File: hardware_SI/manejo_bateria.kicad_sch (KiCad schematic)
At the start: 6 parts

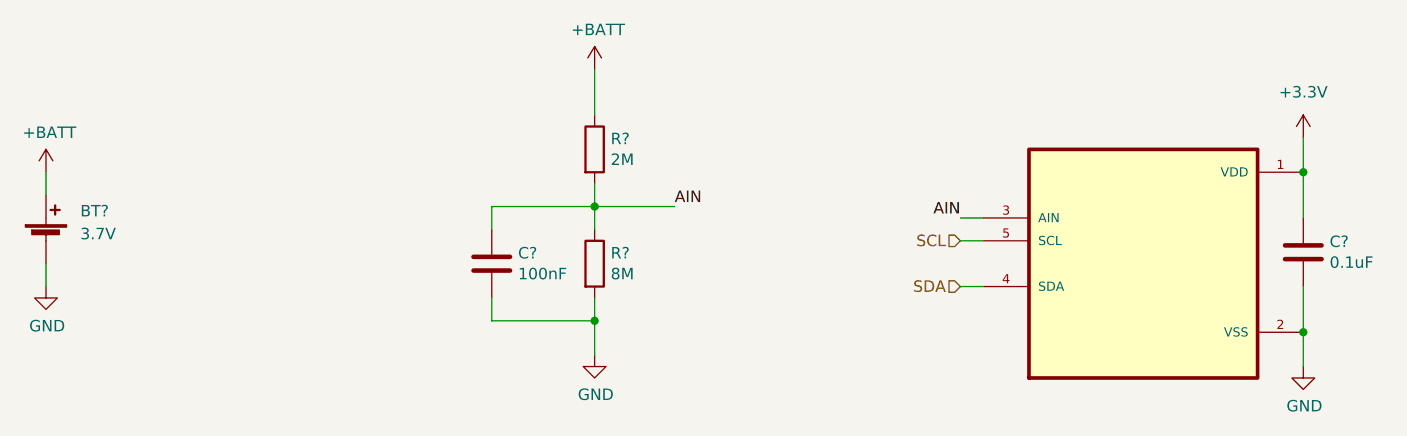
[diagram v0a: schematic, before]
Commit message: Etq compon, C desacop, ferrita
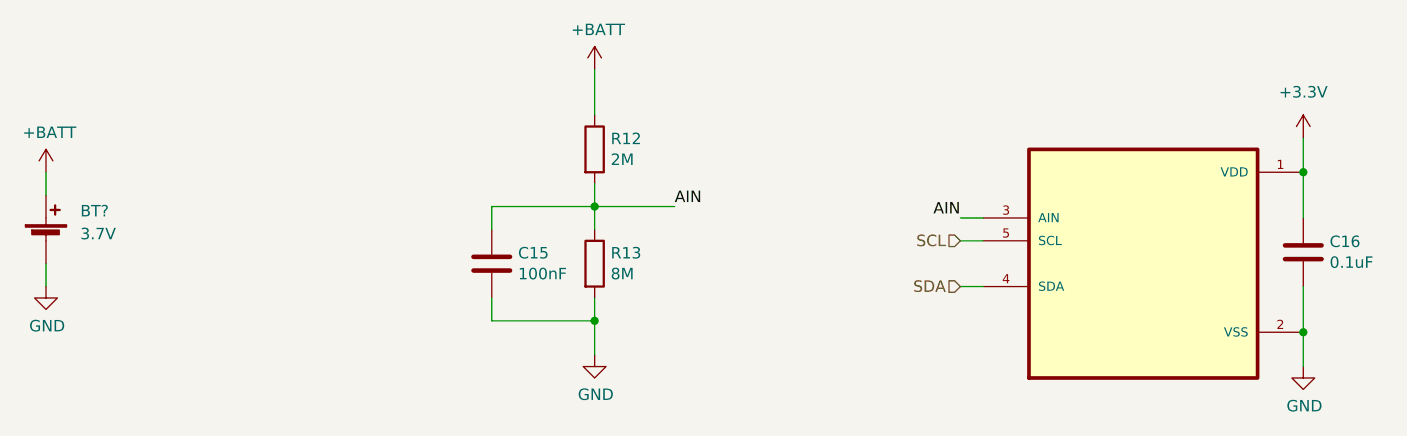
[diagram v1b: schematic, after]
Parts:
- gave numbers to parts that had none: 4
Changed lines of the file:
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@@
   (symbol (lib_id "Device:R") (at 138.43 85.09 0) (unit 1)
     (in_bom yes) (on_board yes)
-    (property "Reference" "R?" (id 0) (at 140.208 83.9216 0)
+    (property "Reference" "R12" (id 0) (at 140.208 83.9216 0)
       (effects (font (size 1.27 1.27)) (justify left))
     )
@@
   (symbol (lib_id "Device:C") (at 217.17 96.52 0) (unit 1)
     (in_bom yes) (on_board yes)
-    (property "Reference" "C?" (id 0) (at 220.091 95.3516 0)
+    (property "Reference" "C16" (id 0) (at 220.091 95.3516 0)
       (effects (font (size 1.27 1.27)) (justify left))
     )
@@
   (symbol (lib_id "Device:R") (at 138.43 97.79 0) (unit 1)
     (in_bom yes) (on_board yes)
-    (property "Reference" "R?" (id 0) (at 140.208 96.6216 0)
+    (property "Reference" "R13" (id 0) (at 140.208 96.6216 0)
       (effects (font (size 1.27 1.27)) (justify left))
     )
@@
   (symbol (lib_id "Device:C") (at 127 97.79 0) (unit 1)
     (in_bom yes) (on_board yes)
-    (property "Reference" "C?" (id 0) (at 129.921 96.6216 0)
+    (property "Reference" "C15" (id 0) (at 129.921 96.6216 0)
       (effects (font (size 1.27 1.27)) (justify left))
     )

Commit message: USB Serial, huellas y correcciones ERC
- Se agregaron componentes para la comunicación serial con la Omega2+.
- Se actualizaron huellas en función de la disponibilidad de los componentes.
- Se ejecutó el ERC y se solucionaron los errores mostrados.
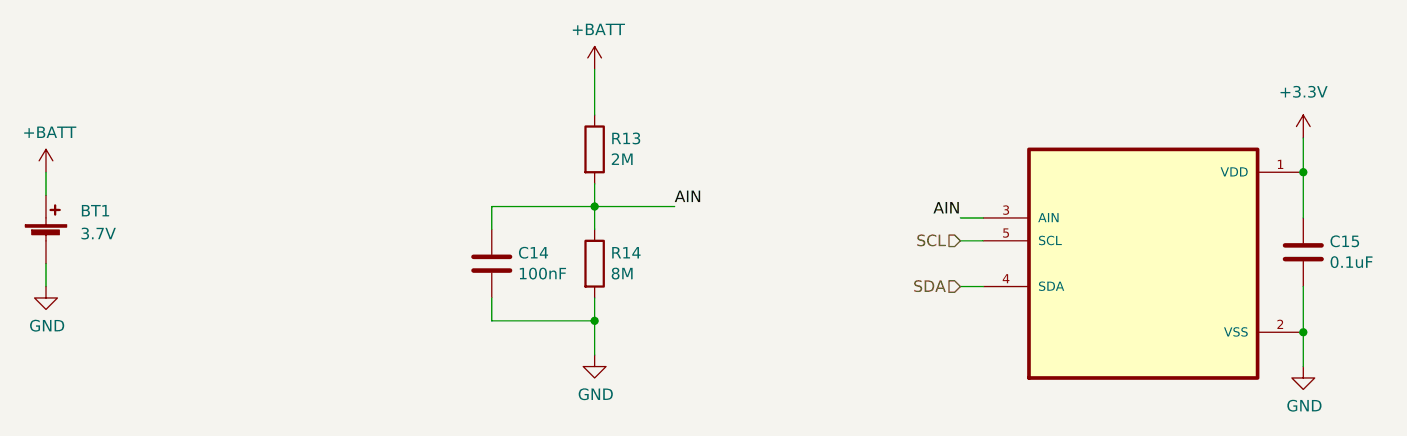
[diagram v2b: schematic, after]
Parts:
- gave numbers to parts that had none: 2
- renumbered C15 to C14, C16 to C15, R12 to R13, R13 to R14
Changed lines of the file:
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@@
   (symbol (lib_id "power:GND") (at 138.43 107.95 0) (unit 1)
     (in_bom yes) (on_board yes)
-    (property "Reference" "#PWR?" (id 0) (at 138.43 114.3 0)
+    (property "Reference" "#PWR038" (id 0) (at 138.43 114.3 0)
       (effects (font (size 1.27 1.27)) hide)
     )
@@
   (symbol (lib_id "Device:Battery_Cell") (at 77.47 95.25 0) (unit 1)
     (in_bom yes) (on_board yes) (fields_autoplaced)
-    (property "Reference" "BT?" (id 0) (at 81.28 91.9479 0)
+    (property "Reference" "BT1" (id 0) (at 81.28 91.9479 0)
       (effects (font (size 1.27 1.27)) (justify left))
     )
@@
       (effects (font (size 1.27 1.27)) (justify left))
     )
-    (property "Footprint" "Battery:BatteryHolder_MPD_BH-18650-PC2" (id 2) (at 77.47 93.726 90)
+    (property "Footprint" "Battery:BatteryHolder_MPD_BH-18650-PC2" (id 2) (at 73.66 93.98 90)
       (effects (font (size 1.27 1.27)) hide)
     )
@@
   (symbol (lib_id "power:GND") (at 77.47 100.33 0) (unit 1)
     (in_bom yes) (on_board yes)
-    (property "Reference" "#PWR?" (id 0) (at 77.47 106.68 0)
+    (property "Reference" "#PWR036" (id 0) (at 77.47 106.68 0)
       (effects (font (size 1.27 1.27)) hide)
     )
@@
   (symbol (lib_id "power:GND") (at 217.17 109.22 0) (unit 1)
     (in_bom yes) (on_board yes)
-    (property "Reference" "#PWR?" (id 0) (at 217.17 115.57 0)
+    (property "Reference" "#PWR040" (id 0) (at 217.17 115.57 0)
       (effects (font (size 1.27 1.27)) hide)
     )
@@
   (symbol (lib_id "power:+BATT") (at 77.47 87.63 0) (unit 1)
     (in_bom yes) (on_board yes)
-    (property "Reference" "#PWR?" (id 0) (at 77.47 91.44 0)
+    (property "Reference" "#PWR035" (id 0) (at 77.47 91.44 0)
       (effects (font (size 1.27 1.27)) hide)
     )
@@
   (symbol (lib_id "Device:R") (at 138.43 85.09 0) (unit 1)
     (in_bom yes) (on_board yes)
-    (property "Reference" "R12" (id 0) (at 140.208 83.9216 0)
+    (property "Reference" "R13" (id 0) (at 140.208 83.9216 0)
       (effects (font (size 1.27 1.27)) (justify left))
     )
@@
   (symbol (lib_id "power:+3.3V") (at 217.17 83.82 0) (unit 1)
     (in_bom yes) (on_board yes) (fields_autoplaced)
-    (property "Reference" "#PWR?" (id 0) (at 217.17 87.63 0)
+    (property "Reference" "#PWR039" (id 0) (at 217.17 87.63 0)
       (effects (font (size 1.27 1.27)) hide)
     )
@@
   (symbol (lib_id "power:+BATT") (at 138.43 76.2 0) (unit 1)
     (in_bom yes) (on_board yes)
-    (property "Reference" "#PWR?" (id 0) (at 138.43 80.01 0)
+    (property "Reference" "#PWR037" (id 0) (at 138.43 80.01 0)
       (effects (font (size 1.27 1.27)) hide)
     )
@@
   (symbol (lib_id "Device:C") (at 217.17 96.52 0) (unit 1)
     (in_bom yes) (on_board yes)
-    (property "Reference" "C16" (id 0) (at 220.091 95.3516 0)
+    (property "Reference" "C15" (id 0) (at 220.091 95.3516 0)
       (effects (font (size 1.27 1.27)) (justify left))
     )
@@
   (symbol (lib_id "Device:R") (at 138.43 97.79 0) (unit 1)
     (in_bom yes) (on_board yes)
-    (property "Reference" "R13" (id 0) (at 140.208 96.6216 0)
+    (property "Reference" "R14" (id 0) (at 140.208 96.6216 0)
       (effects (font (size 1.27 1.27)) (justify left))
     )
@@
   (symbol (lib_id "Device:C") (at 127 97.79 0) (unit 1)
     (in_bom yes) (on_board yes)
-    (property "Reference" "C15" (id 0) (at 129.921 96.6216 0)
+    (property "Reference" "C14" (id 0) (at 129.921 96.6216 0)
       (effects (font (size 1.27 1.27)) (justify left))
     )
@@
   (symbol (lib_id "MCP3021A5T-E_OT:MCP3021A5T-E{slash}OT") (at 199.39 97.79 0) (unit 1)
     (in_bom yes) (on_board yes)
-    (property "Reference" "U?" (id 0) (at 199.39 97.79 0)
+    (property "Reference" "U6" (id 0) (at 199.39 97.79 0)
       (effects (font (size 1.27 1.27)) (justify left bottom) hide)
     )

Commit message: Definiciones PCB
- Se agregan definiciones para la creación de la PCB.
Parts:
- U6: footprint SOT95P270X145-5N -> MCP3021A5T-E_OT:SOT95P270X145-5N
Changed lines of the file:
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@@
       (effects (font (size 1.27 1.27)) (justify left bottom) hide)
     )
-    (property "Footprint" "SOT95P270X145-5N" (id 2) (at 199.39 97.79 0)
+    (property "Footprint" "MCP3021A5T-E_OT:SOT95P270X145-5N" (id 2) (at 199.39 97.79 0)
       (effects (font (size 1.27 1.27)) (justify left bottom) hide)
     )
